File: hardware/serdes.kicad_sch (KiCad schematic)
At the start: 23 parts, among them Q3 BSS138, U4 CCGM1A1, X2 100 MHz LVDS 3.2x2.5

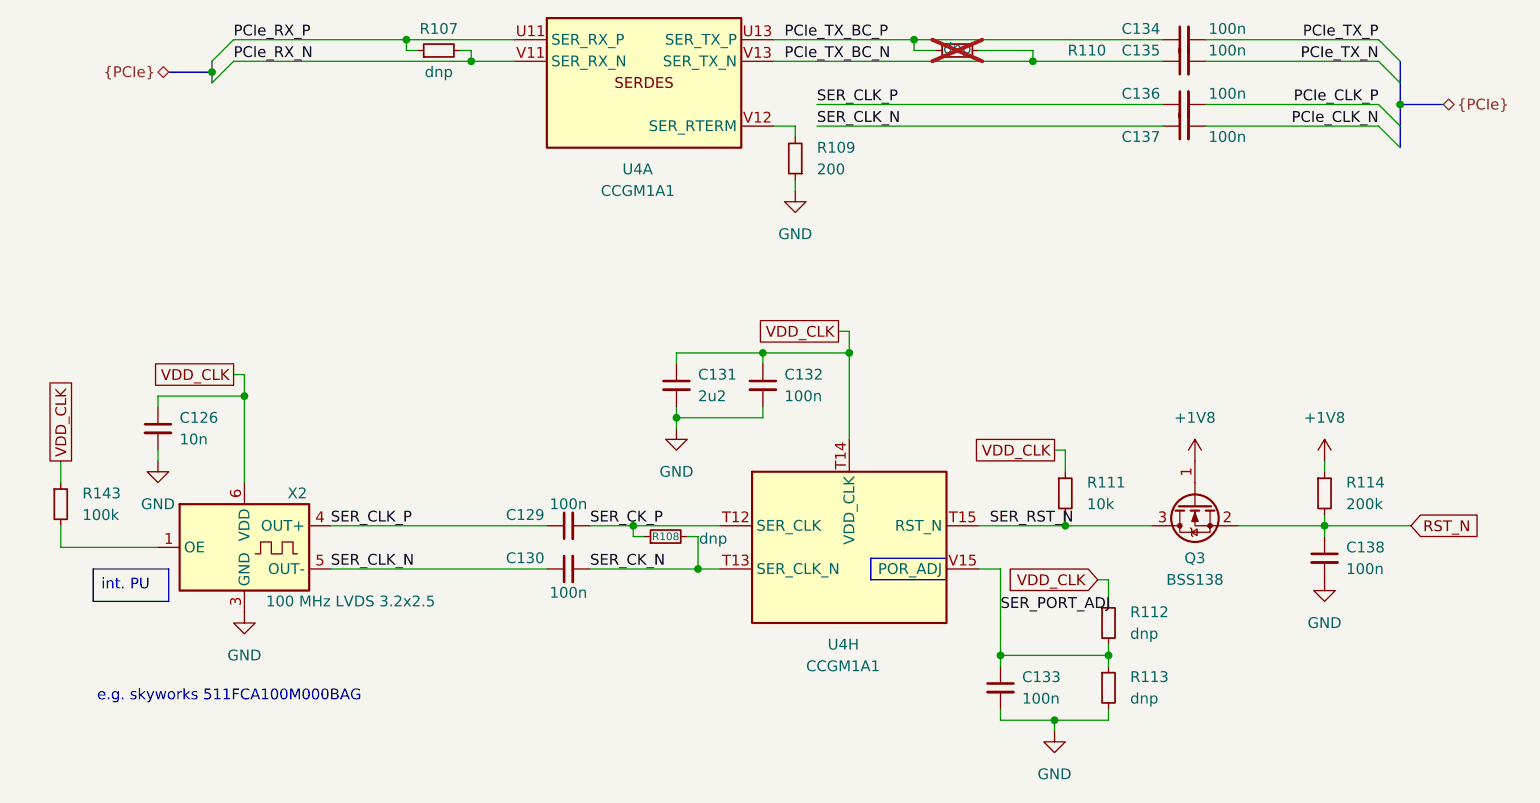
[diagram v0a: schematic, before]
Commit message: Connecting PWR and FAN_PWM to NC pins, using NC3 for Ethernet clock
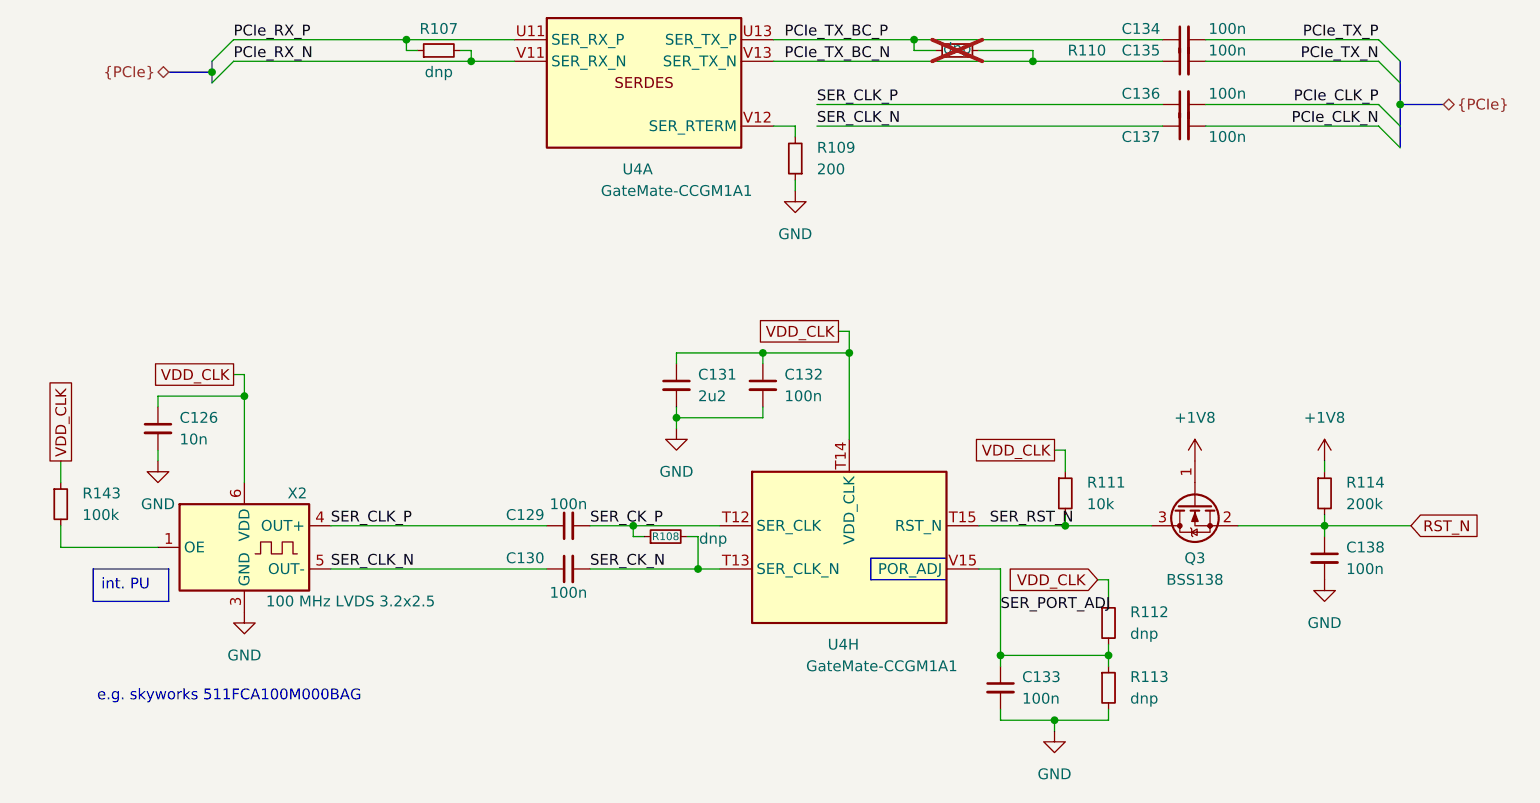
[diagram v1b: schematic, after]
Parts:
- U4: value CCGM1A1 -> GateMate-CCGM1A1
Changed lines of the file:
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@@
 			)
 		)
-		(property "Value" "CCGM1A1"
+		(property "Value" "GateMate-CCGM1A1"
 			(at 104.14 102.87 0)
 			(effects
@@
 			)
 		)
-		(property "Value" "CCGM1A1"
+		(property "Value" "GateMate-CCGM1A1"
 			(at 80.01 46.99 0)
 			(effects

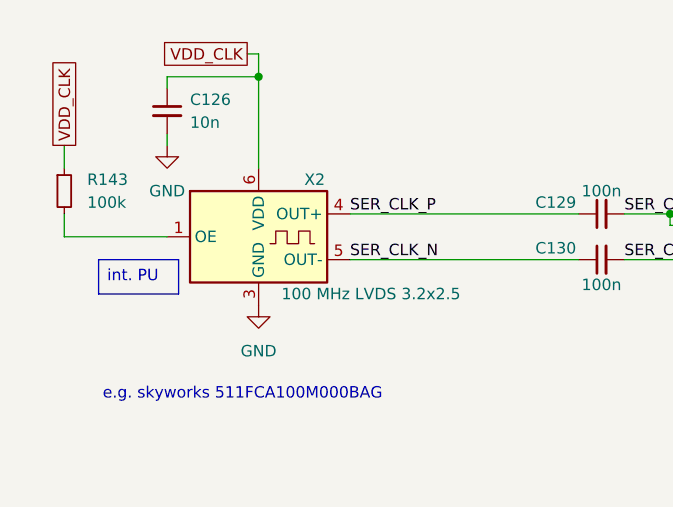
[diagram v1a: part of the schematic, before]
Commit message: Updating sch - moving power select resistors to bottom
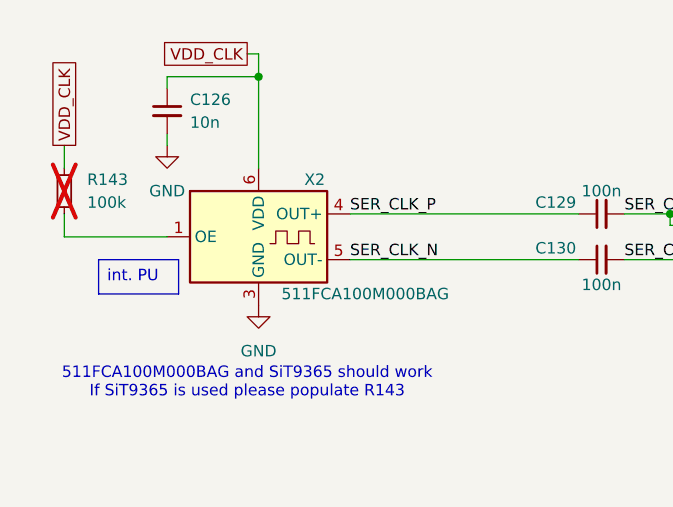
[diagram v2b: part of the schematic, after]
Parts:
- R143: now not fitted
- X2: value 100 MHz LVDS 3.2x2.5 -> 511FCA100M000BAG
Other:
- note added: "511FCA100M000BAG and SiT9365 should work If SiT9365 is used please populate R143"
- note removed: "e.g. skyworks 511FCA100M000BAG"
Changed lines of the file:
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@@
 		)
 	)
-	(text "e.g. skyworks 511FCA100M000BAG"
+	(text "511FCA100M000BAG and SiT9365 should work\nIf SiT9365 is used please populate R143"
 		(exclude_from_sim no)
-		(at 36.322 106.426 0)
+		(at 36.83 105.156 0)
 		(effects
 			(font
@@
 		(in_bom yes)
 		(on_board yes)
-		(dnp no)
+		(dnp yes)
 		(fields_autoplaced yes)
 		(property "Reference" "R143"
@@
 			)
 		)
-		(property "Value" "100 MHz LVDS 3.2x2.5"
+		(property "Value" "511FCA100M000BAG"
 			(at 40.64 95.25 0)
 			(effects

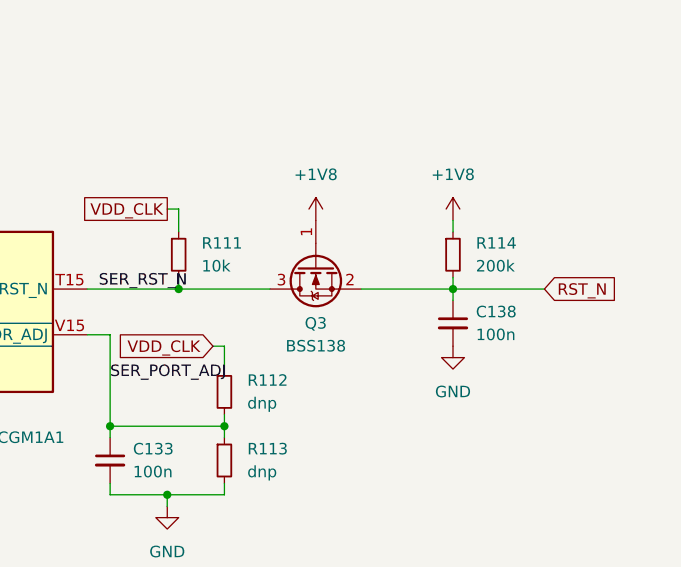
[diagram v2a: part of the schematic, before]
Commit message: Moving VDD_CLK to 1V8, removing 2V5
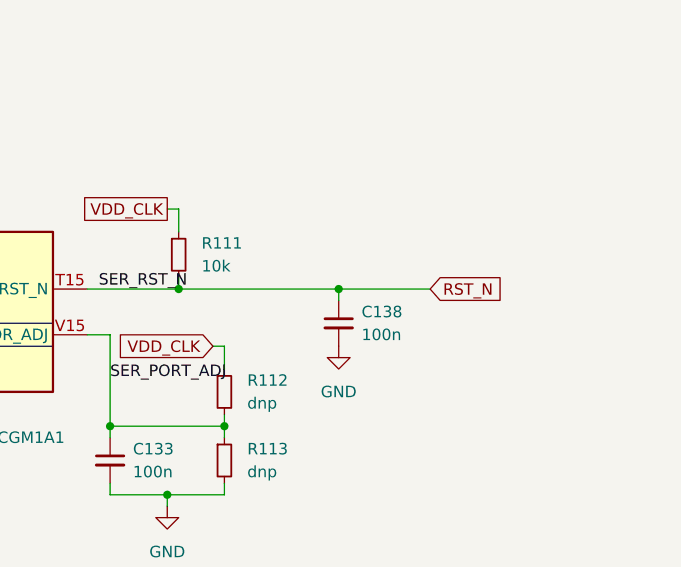
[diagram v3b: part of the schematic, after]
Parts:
- removed Q3: BSS138, Package_TO_SOT_SMD:SOT-523, symbol Transistor_FET:BSS138
- removed R114: 200k, Resistor_SMD:R_0402_1005Metric, symbol Device:R_Small
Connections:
- net SER_RST_N is gone; now on net RST_N: R111.2, U4.T15 (RST_N)
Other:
- moved on the sheet: C138
